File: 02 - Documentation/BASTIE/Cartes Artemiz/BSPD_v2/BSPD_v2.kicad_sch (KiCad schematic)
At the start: 27 parts, among them J1 3P Droit 22-11-2032, J2 3P Droit 22-11-2032, J3 2P Droit 2-11-2022, J4 2P Droit 2-11-2022, K1 SSR CPC1394GR, K2 SSR CPC1394GR

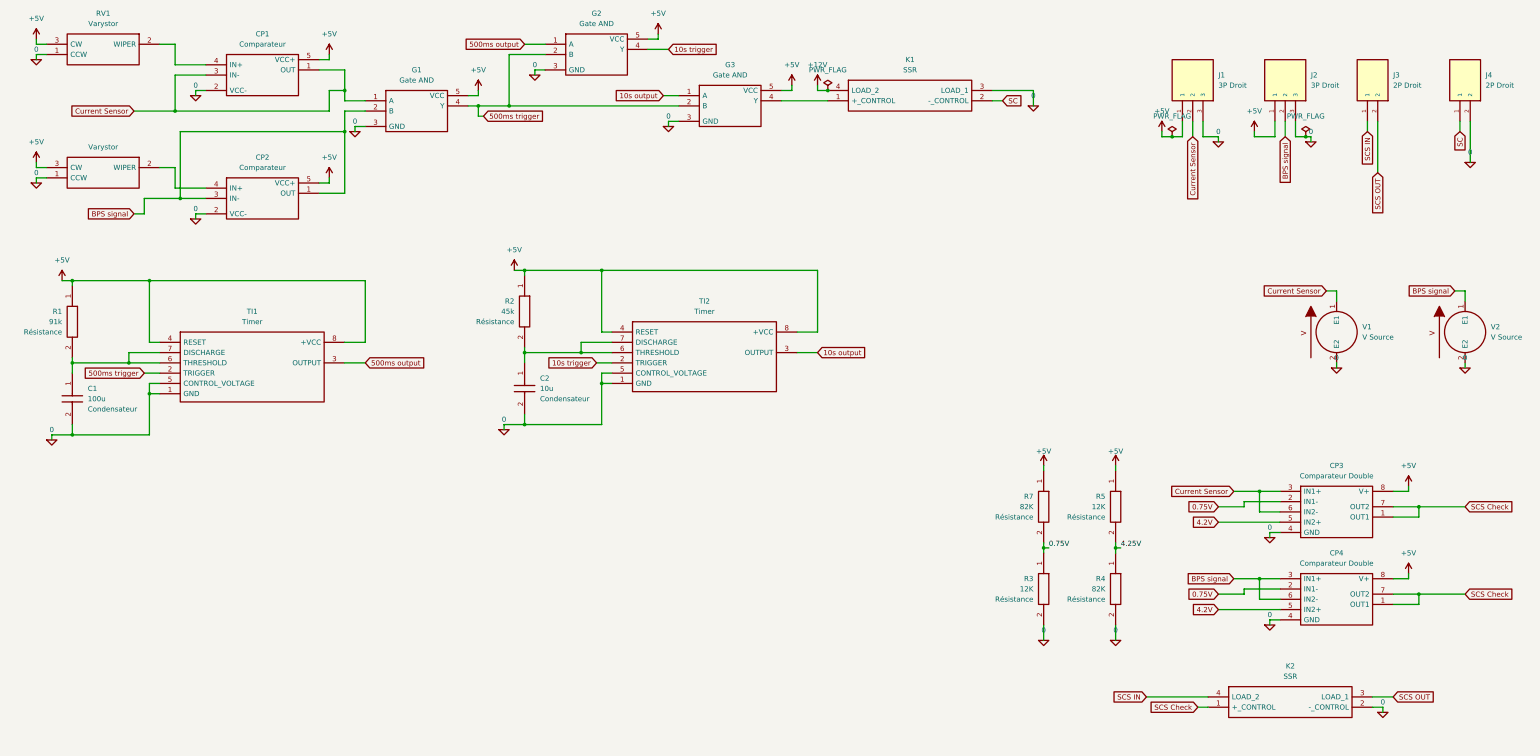
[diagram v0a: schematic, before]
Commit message: BSPD fix
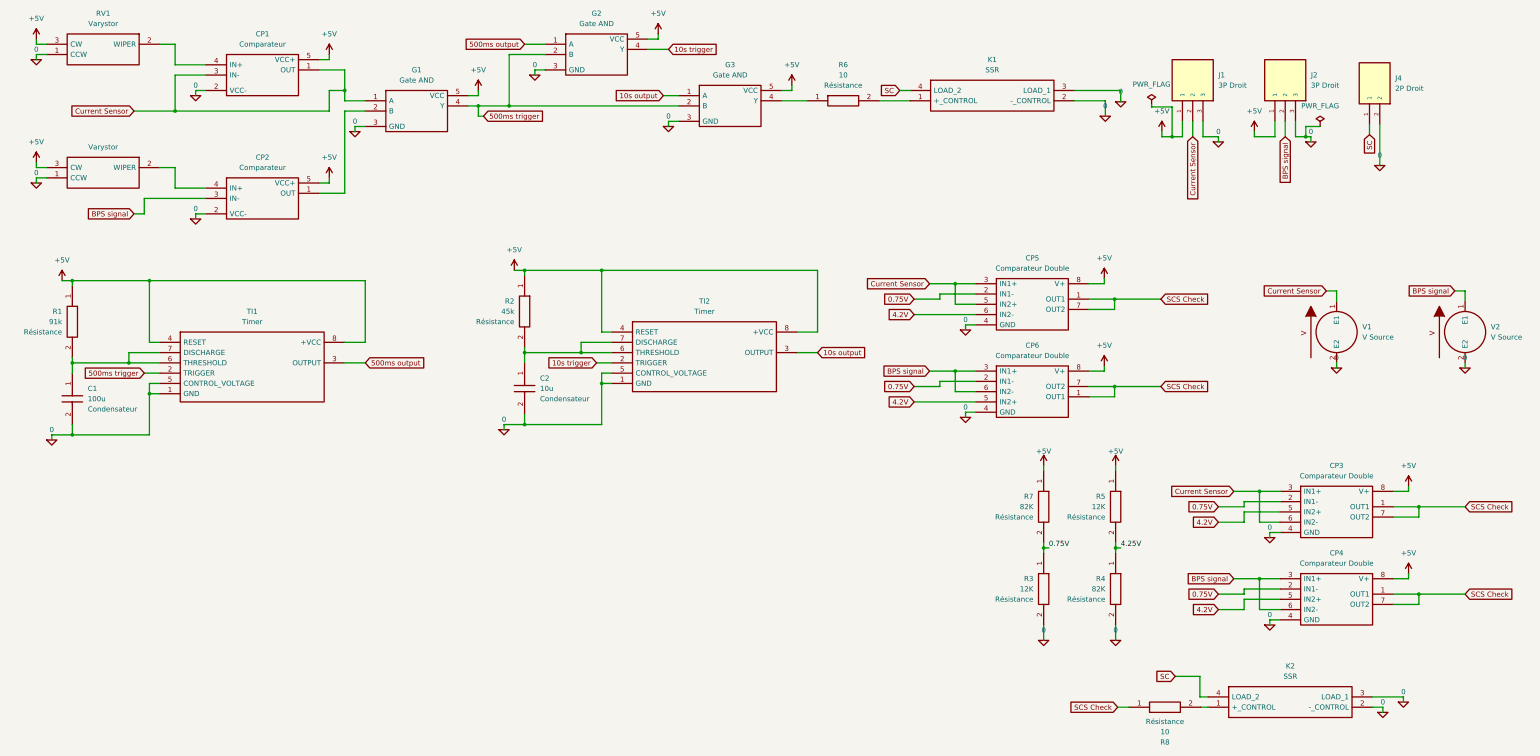
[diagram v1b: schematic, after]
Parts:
- removed J3: 2P Droit 2-11-2022, EPSA_lib:MOLEX_22-11-2022, symbol EPSA_lib:2P Droit 2-11-2022
- added CP5, CP6: Comparateur Double LM393LVDR, EPSA_lib:SOIC127P600X175-8N, symbol EPSA_lib:Dep_ Comparateur Double LM393LVDR
- added R6, R8: 10, EPSA_lib:RESC3216X70N, symbol EPSA_lib:Résistance RK73H2BLTDD2152F
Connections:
- net +12V is gone; now on net SC: K1.4 (LOAD_2)
- net SCS IN is gone; now on net SC: K2.4 (LOAD_2)
- net SCS OUT is gone; now on net 0: K2.3 (LOAD_1)
- net +5V: now also CP5.8 (V+), CP6.8 (V+)
- net 0: now also K1.2 (-_CONTROL), CP5.4 (GND), CP6.4 (GND)
- net 0.75V: now also CP5.2 (IN1-), CP6.2 (IN1-)
- net 4.2V: now also CP5.6 (IN2-), CP6.5 (IN2+)
- net BPS signal: now also CP6.3 (IN1+), CP6.6 (IN2-); no longer CP2.1 (OUT), G1.2 (B)
- net Current Sensor: now also CP5.3 (IN1+), CP5.5 (IN2+)
- net SC: no longer K1.2 (-_CONTROL)
- net SCS Check: now also CP5.1 (OUT1), CP5.7 (OUT2), CP6.1 (OUT1), CP6.7 (OUT2), R8.1; no longer K2.1 (+_CONTROL)
- net at G3.4 (Y): now also R6.1; no longer K1.1 (+_CONTROL)
- new net: K2.1 (+_CONTROL), R8.2
- new net: CP2.1 (OUT), G1.2 (B)
- new net: K1.1 (+_CONTROL), R6.2
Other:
- moved on the sheet: J4, K1
